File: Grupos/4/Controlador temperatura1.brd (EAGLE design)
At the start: 73.3 x 71.1 mm, 13 parts, among them M1 NUCLEO-L452RE, U1 MAX31855KASA+T, X1 1729128

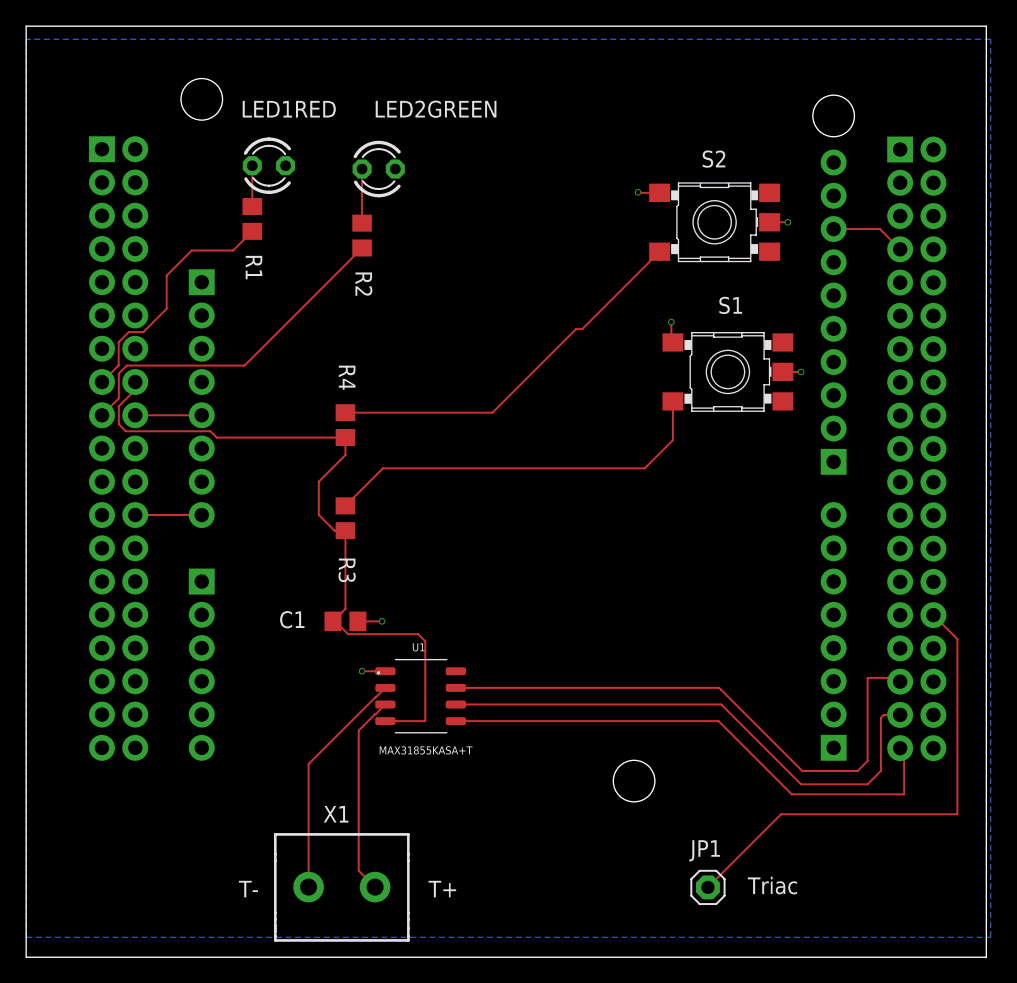
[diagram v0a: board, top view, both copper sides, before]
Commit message: Se agrea el zer-cross, se cambian señales de luar, se arregla el botón
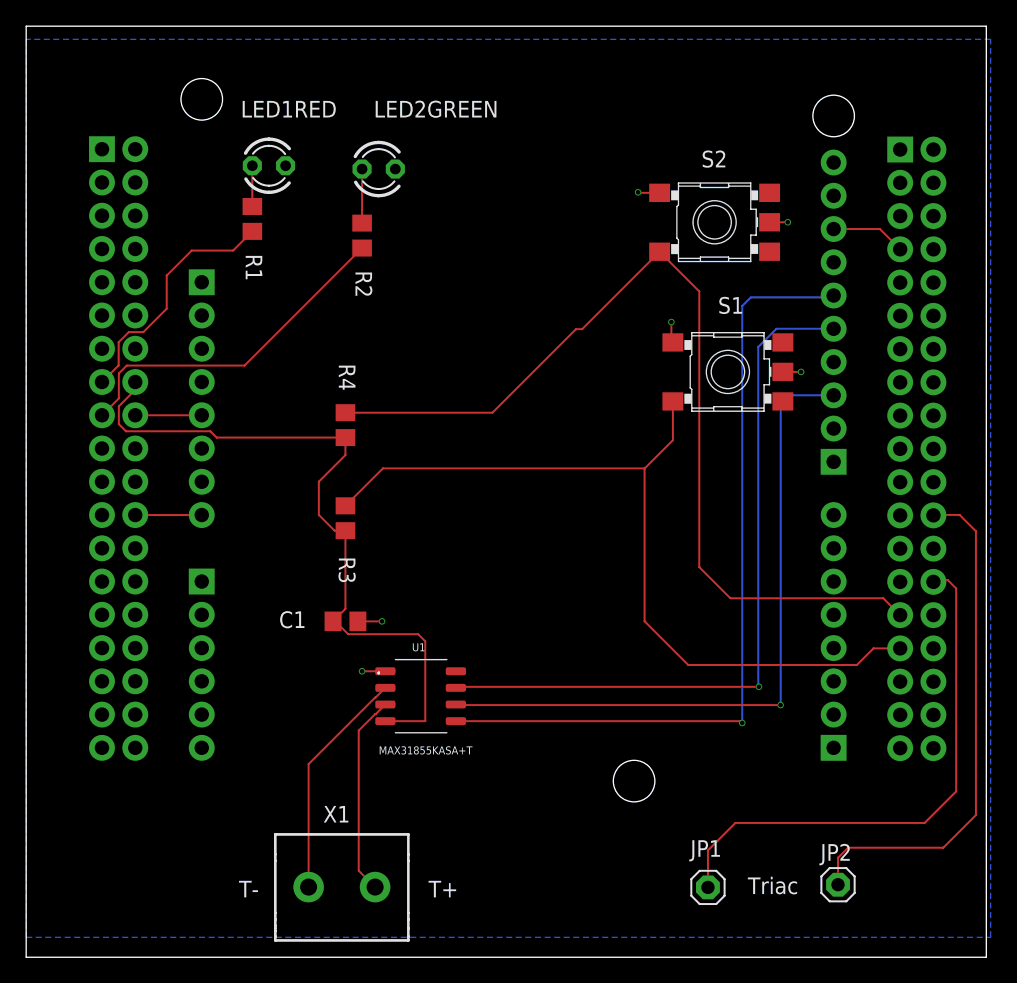
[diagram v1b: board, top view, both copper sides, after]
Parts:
- added JP2: PH1-01-UA, pinhead:1X01
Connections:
- removed net N$12: JP1.1, M1.CN10-30
- new net N$3: JP1.1, M1.CN10-28
- new net N$4: JP2.1, M1.CN10-24
- net CS: now also M1.CN5-3; no longer M1.CN10-35
- net GND: no longer M1.CN10-29, M1.CN10-31
- net N$10: now also M1.CN10-31
- net N$11: now also M1.CN10-29
- net SCK: now also M1.CN5-6; no longer M1.CN10-37
- net SO: now also M1.CN5-5; no longer M1.CN10-33
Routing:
- net N$11: track 29.1 -> 71.3 mm
- net N$3: track 0.00 -> 41.2 mm
- net N$4: track 0.00 -> 40.6 mm
- net N$12: track 37.3 -> 0.00 mm
- net N$10: track 30.1 -> 63.2 mm
- net SCK: track 40.2 -> 62.1 mm, vias 0 -> 1
- net SO: track 43.3 -> 55.5 mm, vias 0 -> 1
- net CS: track 41.0 -> 52.0 mm, vias 0 -> 1
